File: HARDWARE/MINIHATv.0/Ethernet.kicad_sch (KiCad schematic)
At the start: 34 parts, among them J1 8P8C_LED_Shielded, U1 LAN8742A, Y1 Crystal_GND24_Small

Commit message: editorial changes
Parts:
- renumbered C8 to C12, C1 to C13, C2 to C14, C10 to C15, C4 to C16, C5 to C17, C6 to C18, C7 to C19, C3 to C20, J1 to J3, R9 to R10, R2 to R11, R3 to R12, R4 to R13, R5 to R14, R6 to R15, R7 to R16, R8 to R17, R1 to R18, R11 to R19, R12 to R20, R13 to R21, R14 to R22, R17 to R23, R18 to R24, R19 to R25, R20 to R26, R15 to R27, R16 to R28, U1 to U5
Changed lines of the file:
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@@
 		(in_pos_files yes)
 		(dnp no)
-		(property "Reference" "R4"
+		(property "Reference" "R13"
 			(at 69.342 107.188 90)
 			(show_name no)
@@
 		(dnp no)
 		(fields_autoplaced yes)
-		(property "Reference" "#PWR012"
+		(property "Reference" "#PWR045"
 			(at 248.92 88.9 0)
 			(hide yes)
@@
 		(in_pos_files yes)
 		(dnp no)
-		(property "Reference" "R14"
+		(property "Reference" "R22"
 			(at 156.21 95.25 0)
 			(show_name no)
@@
 		(dnp no)
 		(fields_autoplaced yes)
-		(property "Reference" "#PWR021"
+		(property "Reference" "#PWR028"
 			(at 21.59 77.47 0)
 			(hide yes)
@@
 		(dnp no)
 		(fields_autoplaced yes)
-		(property "Reference" "#PWR05"
+		(property "Reference" "#PWR032"
 			(at 74.93 165.1 0)
 			(hide yes)
@@
 		(dnp no)
 		(fields_autoplaced yes)
-		(property "Reference" "C3"
+		(property "Reference" "C20"
 			(at 220.98 147.3199 0)
 			(show_name no)
@@
 		(in_pos_files yes)
 		(dnp no)
-		(property "Reference" "#PWR06"
+		(property "Reference" "#PWR034"
 			(at 101.6 87.63 0)
 			(hide yes)
@@
 		(in_pos_files yes)
 		(dnp no)
-		(property "Reference" "R5"
+		(property "Reference" "R14"
 			(at 69.342 109.728 90)
 			(show_name no)
@@
 		(dnp no)
 		(fields_autoplaced yes)
-		(property "Reference" "C7"
+		(property "Reference" "C19"
 			(at 217.17 63.4999 0)
 			(show_name no)
@@
 		(in_pos_files yes)
 		(dnp no)
-		(property "Reference" "R20"
+		(property "Reference" "R26"
 			(at 230.886 133.604 0)
 			(show_name no)
@@
 		(dnp no)
 		(fields_autoplaced yes)
-		(property "Reference" "C2"
+		(property "Reference" "C14"
 			(at 78.74 151.1299 0)
 			(show_name no)
@@
 		(dnp no)
 		(fields_autoplaced yes)
-		(property "Reference" "C8"
+		(property "Reference" "C12"
 			(at 34.29 62.2299 0)
 			(show_name no)
@@
 		(dnp no)
 		(fields_autoplaced yes)
-		(property "Reference" "C10"
+		(property "Reference" "C15"
 			(at 91.44 77.4699 0)
 			(show_name no)
@@
 		(dnp no)
 		(fields_autoplaced yes)
-		(property "Reference" "#PWR011"
+		(property "Reference" "#PWR046"
 			(at 276.86 107.95 0)
 			(hide yes)
@@
 		(in_pos_files yes)
 		(dnp no)
-		(property "Reference" "R19"
+		(property "Reference" "R25"
 			(at 217.932 133.604 0)
 			(show_name no)
@@
 		(in_pos_files yes)
 		(dnp no)
-		(property "Reference" "R7"
+		(property "Reference" "R16"
 			(at 69.342 114.808 90)
 			(show_name no)
@@
 		(in_pos_files yes)
 		(dnp no)
-		(property "Reference" "R3"
+		(property "Reference" "R12"
 			(at 69.342 104.648 90)
 			(show_name no)
@@
 		(in_pos_files yes)
 		(dnp no)
-		(property "Reference" "#PWR07"
+		(property "Reference" "#PWR035"
 			(at 104.14 87.63 0)
 			(hide yes)
@@
 		(in_pos_files yes)
 		(dnp no)
-		(property "Reference" "R8"
+		(property "Reference" "R17"
 			(at 69.342 117.348 90)
 			(show_name no)
@@
 		(dnp no)
 		(fields_autoplaced yes)
-		(property "Reference" "#PWR014"
+		(property "Reference" "#PWR039"
 			(at 173.99 143.51 0)
 			(hide yes)
@@
 		(dnp no)
 		(fields_autoplaced yes)
-		(property "Reference" "#PWR01"
+		(property "Reference" "#PWR031"
 			(at 63.5 158.75 0)
 			(hide yes)
@@
 		(in_pos_files yes)
 		(dnp no)
-		(property "Reference" "R15"
+		(property "Reference" "R27"
 			(at 263.652 110.236 90)
 			(show_name no)
@@
 		(dnp no)
 		(fields_autoplaced yes)
-		(property "Reference" "#PWR016"
+		(property "Reference" "#PWR041"
 			(at 201.93 76.2 0)
 			(hide yes)
@@
 		(dnp no)
 		(fields_autoplaced yes)
-		(property "Reference" "U1"
+		(property "Reference" "U5"
 			(at 106.2833 146.05 0)
 			(show_name no)
@@
 		(in_pos_files yes)
 		(dnp no)
-		(property "Reference" "#PWR023"
+		(property "Reference" "#PWR030"
 			(at 39.37 120.65 0)
 			(hide yes)
@@
 		(in_pos_files yes)
 		(dnp no)
-		(property "Reference" "#PWR09"
+		(property "Reference" "#PWR038"
 			(at 127 92.71 0)
 			(hide yes)
@@
 		(in_pos_files yes)
 		(dnp no)
-		(property "Reference" "R13"
+		(property "Reference" "R21"
 			(at 148.59 95.25 0)
 			(show_name no)
@@
 		(in_pos_files yes)
 		(dnp no)
-		(property "Reference" "R1"
+		(property "Reference" "R18"
 			(at 128.524 116.078 90)
 			(show_name no)
@@
 		(in_pos_files yes)
 		(dnp no)
-		(property "Reference" "#PWR018"
+		(property "Reference" "#PWR043"
 			(at 213.36 58.42 0)
 			(hide yes)
@@
 		(dnp no)
 		(fields_autoplaced yes)
-		(property "Reference" "C6"
+		(property "Reference" "C18"
 			(at 205.74 63.4999 0)
 			(show_name no)
@@
 		(dnp no)
 		(fields_autoplaced yes)
-		(property "Reference" "#PWR04"
+		(property "Reference" "#PWR029"
 			(at 52.07 165.1 0)
 			(hide yes)
@@
 		(dnp no)
 		(fields_autoplaced yes)
-		(property "Reference" "C5"
+		(property "Reference" "C17"
 			(at 187.96 129.5399 0)
 			(show_name no)
@@
 		(in_pos_files yes)
 		(dnp no)
-		(property "Reference" "R2"
+		(property "Reference" "R11"
 			(at 69.342 102.108 90)
 			(show_name no)
@@
 		(dnp no)
 		(fields_autoplaced yes)
-		(property "Reference" "#PWR03"
+		(property "Reference" "#PWR037"
 			(at 142.24 120.65 0)
 			(hide yes)
@@
 		(in_pos_files yes)
 		(dnp no)
-		(property "Reference" "#PWR019"
+		(property "Reference" "#PWR040"
 			(at 173.99 58.42 0)
 			(hide yes)
@@
 		(dnp no)
 		(fields_autoplaced yes)
-		(property "Reference" "#PWR02"
+		(property "Reference" "#PWR036"
 			(at 104.14 156.21 0)
 			(hide yes)
@@
 		(in_pos_files yes)
 		(dnp no)
-		(property "Reference" "#PWR020"
+		(property "Reference" "#PWR027"
 			(at 21.59 58.42 0)
 			(hide yes)
@@
 		(in_pos_files yes)
 		(dnp no)
-		(property "Reference" "R12"
+		(property "Reference" "R20"
 			(at 140.97 95.25 0)
 			(show_name no)
@@
 		(in_pos_files yes)
 		(dnp no)
-		(property "Reference" "#PWR017"
+		(property "Reference" "#PWR042"
 			(at 213.36 76.2 0)
 			(hide yes)
@@
 		(in_pos_files yes)
 		(dnp no)
-		(property "Reference" "R11"
+		(property "Reference" "R19"
 			(at 133.35 95.25 0)
 			(show_name no)
@@
 		(in_pos_files yes)
 		(dnp no)
-		(property "Reference" "R17"
+		(property "Reference" "R23"
 			(at 200.152 133.604 0)
 			(show_name no)
@@
 		(dnp no)
 		(fields_autoplaced yes)
-		(property "Reference" "C4"
+		(property "Reference" "C16"
 			(at 177.8 129.5399 0)
 			(show_name no)
@@
 		(dnp no)
 		(fields_autoplaced yes)
-		(property "Reference" "#PWR010"
+		(property "Reference" "#PWR047"
 			(at 276.86 123.19 0)
 			(hide yes)
@@
 		(dnp no)
 		(fields_autoplaced yes)
-		(property "Reference" "C1"
+		(property "Reference" "C13"
 			(at 55.88 151.1299 0)
 			(show_name no)
@@
 		(dnp no)
 		(fields_autoplaced yes)
-		(property "Reference" "#PWR013"
+		(property "Reference" "#PWR044"
 			(at 217.17 161.29 0)
 			(hide yes)
@@
 		(in_pos_files yes)
 		(dnp no)
-		(property "Reference" "R18"
+		(property "Reference" "R24"
 			(at 213.106 133.604 0)
 			(show_name no)
@@
 		(in_pos_files yes)
 		(dnp no)
-		(property "Reference" "J1"
+		(property "Reference" "J3"
 			(at 248.92 130.81 0)
 			(show_name no)
@@
 		(in_pos_files yes)
 		(dnp no)
-		(property "Reference" "#PWR08"
+		(property "Reference" "#PWR033"
 			(at 99.06 68.58 0)
 			(hide yes)
@@
 		(in_pos_files yes)
 		(dnp no)
-		(property "Reference" "R6"
+		(property "Reference" "R15"
 			(at 69.342 112.268 90)
 			(show_name no)
@@
 		(in_pos_files yes)
 		(dnp no)
-		(property "Reference" "R16"
+		(property "Reference" "R28"
 			(at 265.176 125.222 90)
 			(show_name no)
@@
 		(dnp no)
 		(fields_autoplaced yes)
-		(property "Reference" "R9"
+		(property "Reference" "R10"
 			(at 40.64 114.3 90)
 			(show_name no)

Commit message: added ltdc bus to mcu page, editoral change to rmii bus
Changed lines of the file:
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@@
 		)
 	)
-	(hierarchical_label "RMII{TXD0 TXD1 TXDEN RXD0 RXD1 RXER CRS_DV MDIO MDC REFCLK}"
+	(hierarchical_label "{RMII}"
 		(shape input)
 		(at 86.36 20.32 180)

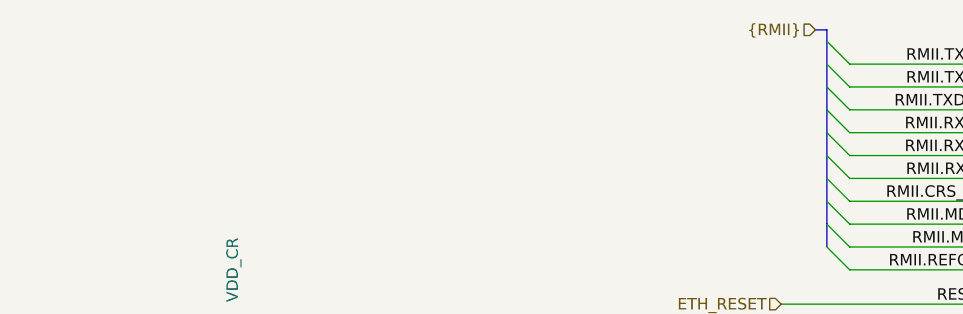
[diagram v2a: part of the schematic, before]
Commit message: mcu pwr/vcap ports, hdmi gpio, buses
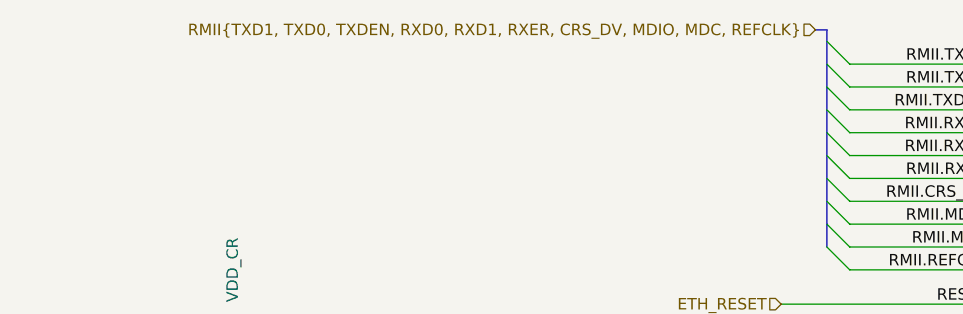
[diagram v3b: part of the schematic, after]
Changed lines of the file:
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@@
 		)
 	)
-	(hierarchical_label "{RMII}"
+	(hierarchical_label "RMII{TXD1, TXD0, TXDEN, RXD0, RXD1, RXER, CRS_DV, MDIO, MDC, REFCLK}"
 		(shape input)
 		(at 86.36 20.32 180)
